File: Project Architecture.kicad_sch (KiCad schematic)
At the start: 0 parts

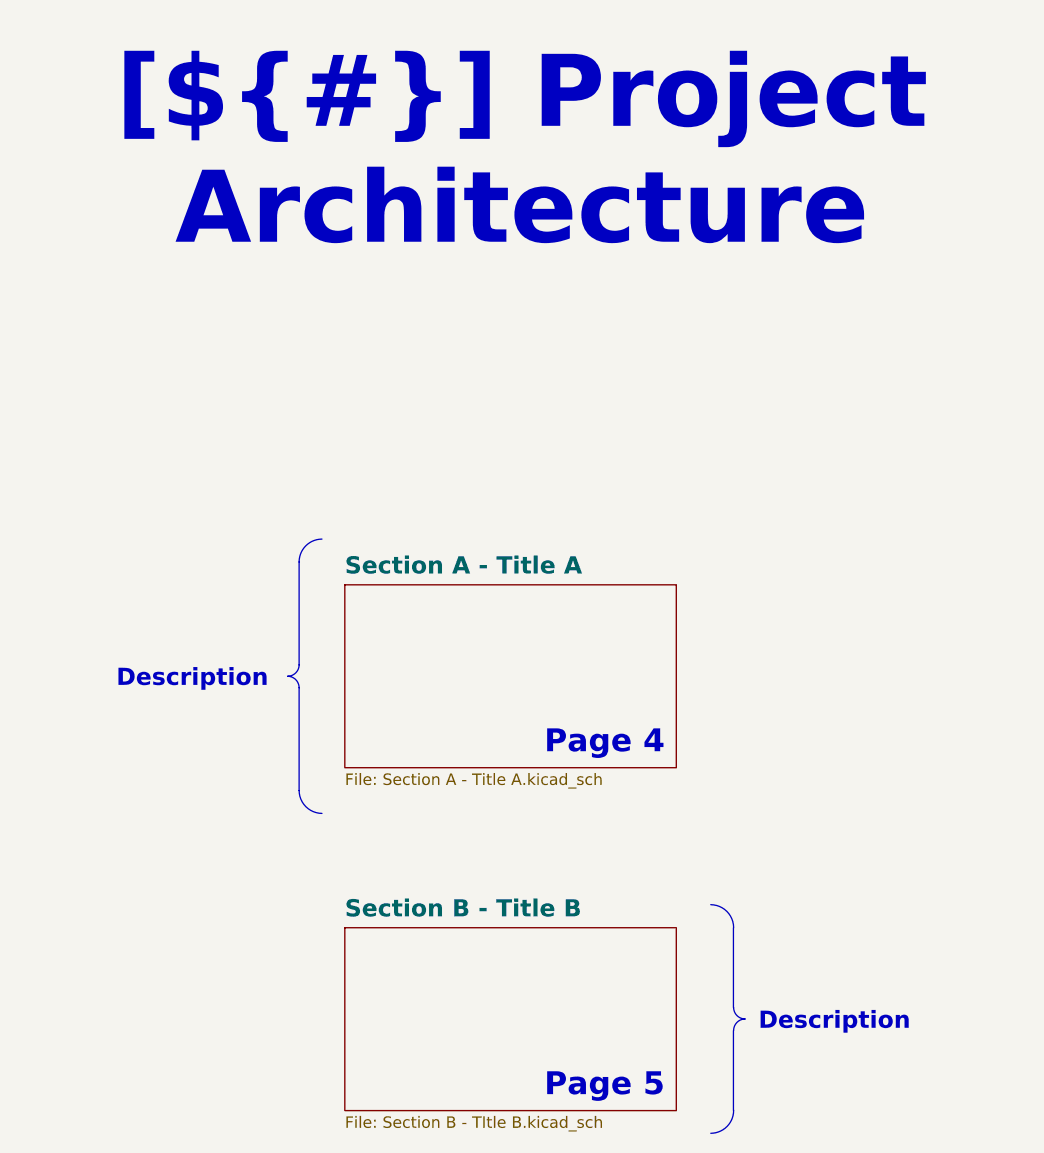
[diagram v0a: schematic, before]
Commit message: [added] completed initial sch design, move from draft to preliminary
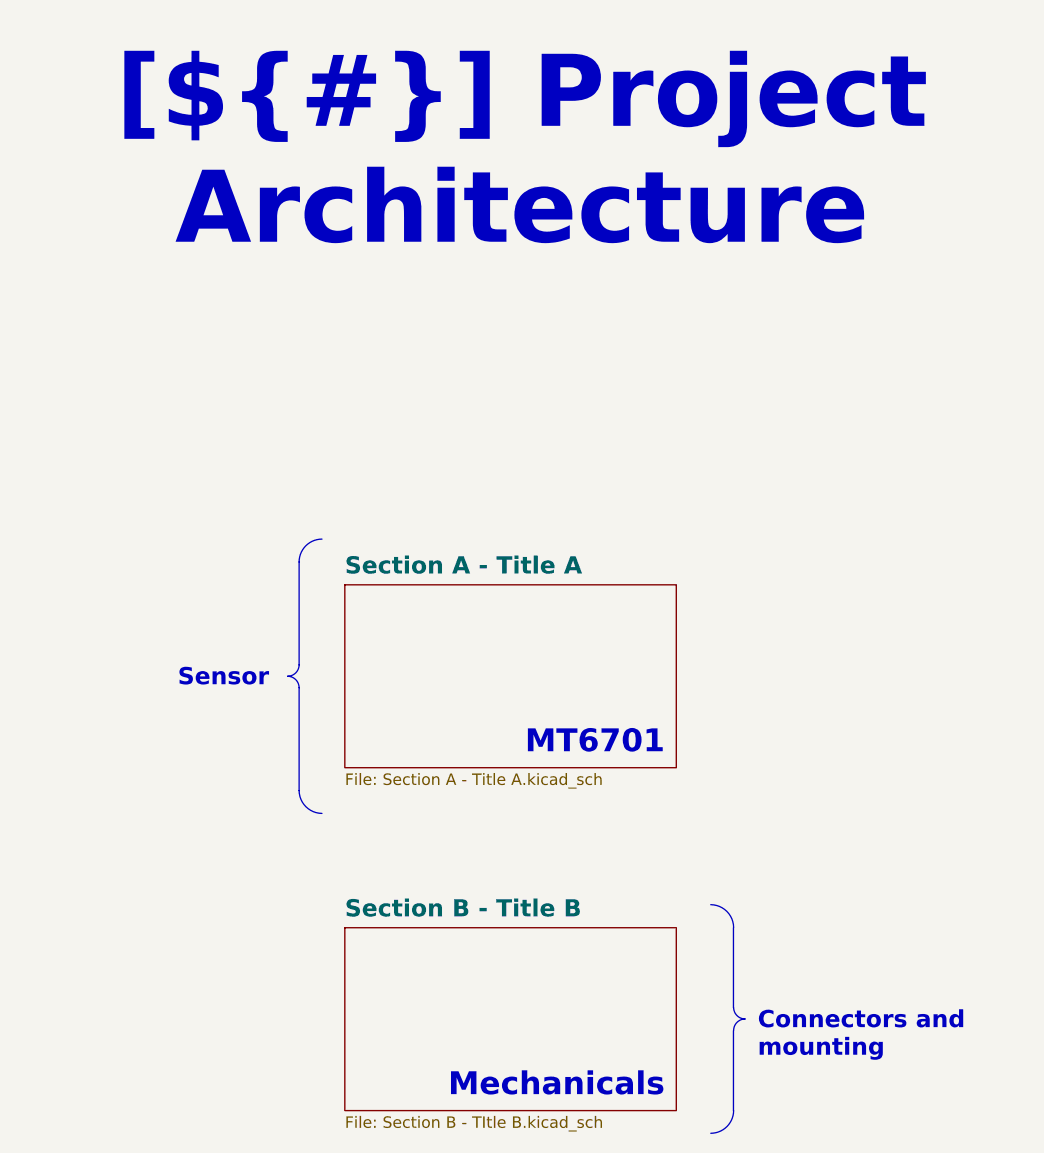
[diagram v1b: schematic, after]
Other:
- note added: "MT6701"
- note added: "Mechanicals"
- note removed: "Page 4"
- note removed: "Page 5"
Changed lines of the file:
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@@
 (kicad_sch
-	(version 20231120)
+	(version 20250114)
 	(generator "eeschema")
-	(generator_version "8.0")
+	(generator_version "9.0")
 	(paper "A3")
 	(title_block
@@
 		(company "${COMPANY}")
 	)
+	(arc
+		(start 185.42 85.09)
+		(mid 185.0451 85.9851)
+		(end 184.15 86.36)
+		(stroke
+			(width 0)
+			(type default)
+		)
+		(fill
+			(type none)
+		)
+	)
+	(arc
+		(start 234.97 124.44)
+		(mid 234.0749 124.0651)
+		(end 233.7 123.17)
+		(stroke
+			(width 0)
+			(type default)
+		)
+		(fill
+			(type none)
+		)
+	)
+	(arc
+		(start 233.7 125.71)
+		(mid 234.0749 124.8149)
+		(end 234.97 124.44)
+		(stroke
+			(width 0)
+			(type default)
+		)
+		(fill
+			(type none)
+		)
+	)
+	(arc
+		(start 233.7 134.6)
+		(mid 232.9561 136.3961)
+		(end 231.16 137.14)
+		(stroke
+			(width 0)
+			(type default)
+		)
+		(fill
+			(type none)
+		)
+	)
+	(arc
+		(start 184.15 86.36)
+		(mid 185.0451 86.7349)
+		(end 185.42 87.63)
+		(stroke
+			(width 0)
+			(type default)
+		)
+		(fill
+			(type none)
+		)
+	)
+	(arc
+		(start 187.96 101.6)
+		(mid 186.1698 100.8502)
+		(end 185.42 99.06)
+		(stroke
+			(width 0)
+			(type default)
+		)
+		(fill
+			(type none)
+		)
+	)
+	(arc
+		(start 231.16 111.74)
+		(mid 232.9502 112.4898)
+		(end 233.7 114.28)
+		(stroke
+			(width 0)
+			(type default)
+		)
+		(fill
+			(type none)
+		)
+	)
+	(arc
+		(start 185.42 73.66)
+		(mid 186.1639 71.8639)
+		(end 187.96 71.12)
+		(stroke
+			(width 0)
+			(type default)
+		)
+		(fill
+			(type none)
+		)
+	)
+	(text "Mechanicals"
+		(exclude_from_sim no)
+		(at 226.06 133.35 0)
+		(effects
+			(font
+				(size 2.54 2.54)
+				(bold yes)
+				(color 100 70 50 1)
+			)
+			(justify right bottom)
+			(href "#5")
+		)
+	)
+	(text "MT6701"
+		(exclude_from_sim no)
+		(at 226.06 95.25 0)
+		(effects
+			(font
+				(size 2.54 2.54)
+				(bold yes)
+				(color 20 60 40 1)
+			)
+			(justify right bottom)
+			(href "#4")
+		)
+	)
+	(text_box "Sensor"
+		(exclude_from_sim no)
+		(at 166.37 83.82 0)
+		(size 17.145 5.08)
+		(margins 1.4287 1.4287 1.4287 1.4287)
+		(stroke
+			(width -0.0001)
+			(type solid)
+		)
+		(fill
+			(type none)
+		)
+		(effects
+			(font
+				(size 1.905 1.905)
+				(thickness 0.381)
+				(bold yes)
+				(color 0 0 0 1)
+			)
+			(justify right top)
+		)
+	)
+	(text_box "Connectors and mounting"
+		(exclude_from_sim no)
+		(at 234.95 121.92 0)
+		(size 26.015 5.1)
+		(margins 1.4287 1.4287 1.4287 1.4287)
+		(stroke
+			(width -0.0001)
+			(type solid)
+		)
+		(fill
+			(type none)
+		)
+		(effects
+			(font
+				(size 1.905 1.905)
+				(thickness 0.381)
+				(bold yes)
+				(color 0 0 0 1)
+			)
+			(justify left top)
+		)
+	)
+	(text_box "[${#}] ${TITLE}"
+		(exclude_from_sim no)
+		(at 144.78 21.59 0)
+		(size 130.81 12.7)
+		(margins 5.9999 5.9999 5.9999 5.9999)
+		(stroke
+			(width -0.0001)
+			(type default)
+		)
+		(fill
+			(type none)
+		)
+		(effects
+			(font
+				(face "Times New Roman")
+				(size 8 8)
+				(thickness 1.2)
+				(bold yes)
+				(color 162 22 34 1)
+			)
+		)
+	)
 	(polyline
 		(pts
@@
 		)
 	)
-	(arc
-		(start 185.42 85.09)
-		(mid 185.0451 85.9851)
-		(end 184.15 86.36)
-		(stroke
-			(width 0)
-			(type default)
-		)
-		(fill
-			(type none)
-		)
-	)
-	(arc
-		(start 234.97 124.44)
-		(mid 234.0749 124.0651)
-		(end 233.7 123.17)
-		(stroke
-			(width 0)
-			(type default)
-		)
-		(fill
-			(type none)
-		)
-	)
-	(arc
-		(start 233.7 125.71)
-		(mid 234.0749 124.8149)
-		(end 234.97 124.44)
-		(stroke
-			(width 0)
-			(type default)
-		)
-		(fill
-			(type none)
-		)
-	)
-	(arc
-		(start 233.7 134.6)
-		(mid 232.9561 136.3961)
-		(end 231.16 137.14)
-		(stroke
-			(width 0)
-			(type default)
-		)
-		(fill
-			(type none)
-		)
-	)
-	(arc
-		(start 184.15 86.36)
-		(mid 185.0451 86.7349)
-		(end 185.42 87.63)
-		(stroke
-			(width 0)
-			(type default)
-		)
-		(fill
-			(type none)
-		)
-	)
-	(arc
-		(start 187.96 101.6)
-		(mid 186.1698 100.8502)
-		(end 185.42 99.06)
-		(stroke
-			(width 0)
-			(type default)
-		)
-		(fill
-			(type none)
-		)
-	)
-	(arc
-		(start 231.16 111.74)
-		(mid 232.9502 112.4898)
-		(end 233.7 114.28)
-		(stroke
-			(width 0)
-			(type default)
-		)
-		(fill
-			(type none)
-		)
-	)
-	(arc
-		(start 185.42 73.66)
-		(mid 186.1639 71.8639)
-		(end 187.96 71.12)
-		(stroke
-			(width 0)
-			(type default)
-		)
-		(fill
-			(type none)
-		)
-	)
-	(text_box "Description"
-		(exclude_from_sim no)
-		(at 166.37 83.82 0)
-		(size 17.145 5.08)
-		(stroke
-			(width -0.0001)
-			(type default)
-		)
-		(fill
-			(type none)
-		)
-		(effects
-			(font
-				(size 1.905 1.905)
-				(thickness 0.381)
-				(bold yes)
-				(color 0 0 0 1)
-			)
-			(justify right top)
-		)
-	)
-	(text_box "Description"
-		(exclude_from_sim no)
-		(at 234.95 121.92 0)
-		(size 26.015 5.1)
-		(stroke
-			(width -0.0001)
-			(type default)
-		)
-		(fill
-			(type none)
-		)
-		(effects
-			(font
-				(size 1.905 1.905)
-				(thickness 0.381)
-				(bold yes)
-				(color 0 0 0 1)
-			)
-			(justify left top)
-		)
-	)
-	(text_box "[${#}] ${TITLE}"
-		(exclude_from_sim no)
-		(at 144.78 21.59 0)
-		(size 130.81 12.7)
-		(stroke
-			(width -0.0001)
-			(type default)
-		)
-		(fill
-			(type none)
-		)
-		(effects
-			(font
-				(face "Times New Roman")
-				(size 8 8)
-				(thickness 1.2)
-				(bold yes)
-				(color 162 22 34 1)
-			)
-		)
-	)
-	(text "Page 5"
-		(exclude_from_sim no)
-		(at 226.06 133.35 0)
-		(effects
-			(font
-				(size 2.54 2.54)
-				(bold yes)
-				(color 100 70 50 1)
-			)
-			(justify right bottom)
-			(href "#5")
-		)
-	)
-	(text "Page 4"
-		(exclude_from_sim no)
-		(at 226.06 95.25 0)
-		(effects
-			(font
-				(size 2.54 2.54)
-				(bold yes)
-				(color 20 60 40 1)
-			)
-			(justify right bottom)
-			(href "#4")
-		)
-	)
 	(sheet
 		(at 190.5 114.3)
 		(size 36.83 20.32)
+		(exclude_from_sim no)
+		(in_bom yes)
+		(on_board yes)
+		(dnp no)
 		(fields_autoplaced yes)
 		(stroke
@@
 		)
 		(instances
-			(project "KDT_Hierarchical_KiBot"
+			(project "kibot-test-cicd"
 				(path "/f9e05184-c88b-4a88-ae9c-ab2bdb32be7c/c5103ceb-5325-4a84-a025-9638a412984e"
 					(page "5")
@@
 		(at 190.5 76.2)
 		(size 36.83 20.32)
+		(exclude_from_sim no)
+		(in_bom yes)
+		(on_board yes)
+		(dnp no)
 		(fields_autoplaced yes)
 		(stroke
@@
 		)
 		(instances
-			(project "KDT_Hierarchical_KiBot"
+			(project "kibot-test-cicd"
 				(path "/f9e05184-c88b-4a88-ae9c-ab2bdb32be7c/c5103ceb-5325-4a84-a025-9638a412984e"
 					(page "4")
